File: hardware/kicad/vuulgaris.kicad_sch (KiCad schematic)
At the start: 269 parts, among them J1 TFPUSH, J10 PJ-603_C41409498, J11 TYPE-C-31-M-12, J12 FACEPLATE 2x5 IDC, J2 PJ-376, J3 PJ-376, J4 PJ-376, J5 PJ-376, J7 PJ-603_C41409498, J8 PJ-603_C41409498, J9 PJ-603_C41409498, Q1 J113 / MMBFJ113, Q2 J113 / MMBFJ113, SW1 SW_DPDT_FLAT, SW2 SW_DPDT_FLAT, SW4 12x12 tactile, SW5 12x12 tactile, SW6 12x12 tactile, SW7 12x12 tactile, SW8 12x12 tactile, SW9 12x12 tactile, U1 ES_DAISY_PATCH_SM_REV1, U101 V3205SD, U102 TL072_FLAT, U103 TL072_FLAT, U104 CD4046B, U106 TL072_FLAT, U201 V3205SD, U202 TL072_FLAT, U203 TL072_FLAT, U204 CD4046B, U206 TL072_FLAT, U3 MCP23017-E_SO, U301 TL084, U302 TL074, U4 MCP23017-E_SO, U401 TL084, U402 TL074, U5 AMS1117-3.3, U6 AMS1117-3.3, U7 DKM10E-12, U8 78L05

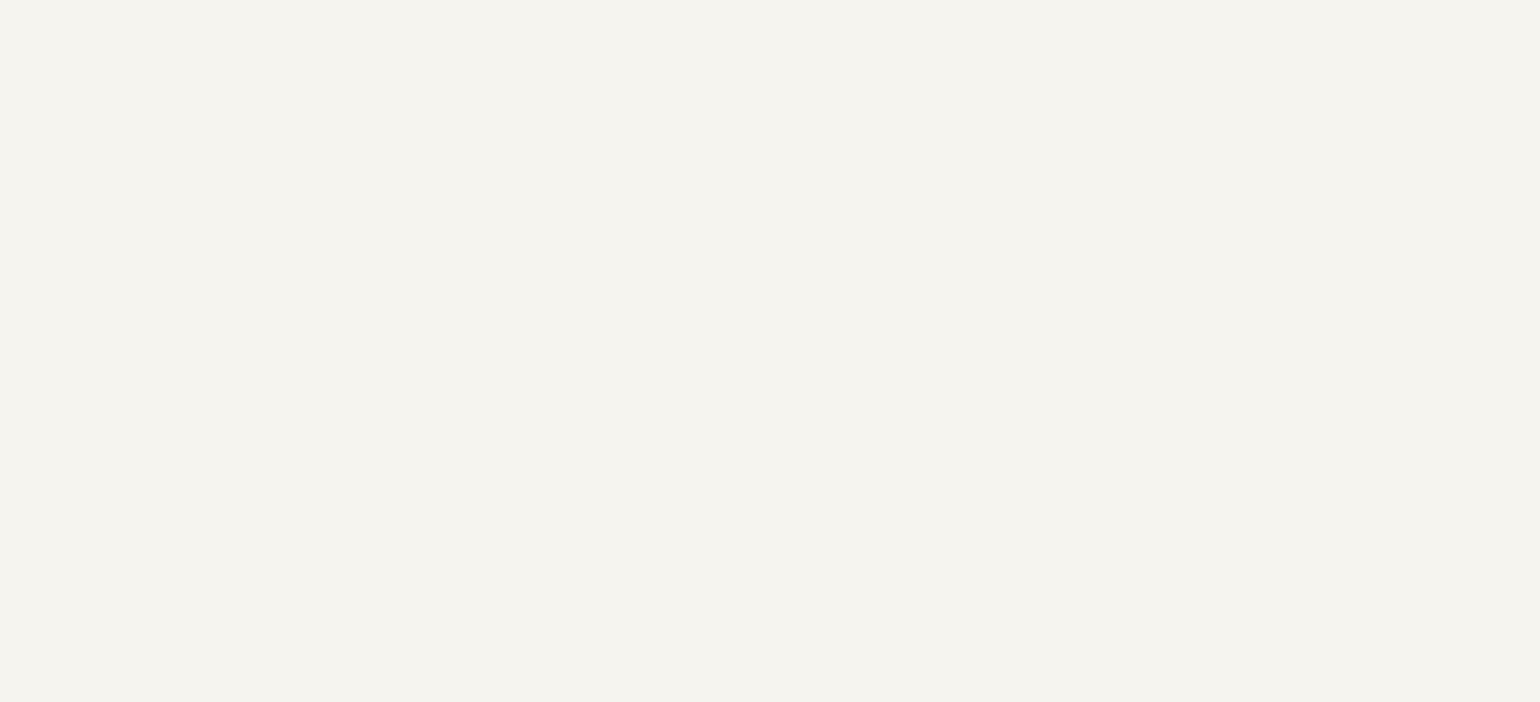
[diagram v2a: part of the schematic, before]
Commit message: hardware: ten signal test points, TP6-TP15
BBD_DRY and BBD_SIGIN per channel (the mki manual's TP1/TP3, asked for in
bbd-mki.md so R104's value can be chosen with a scope rather than by ear), the
vactrol LED drive per channel (RT301/RT401 are hand-trimmed and you cannot set a
trimmer you cannot measure), both 4046 clocks (their mistracking is the stereo
width), and the two DAC outputs (splits a fault into firmware or analog).

Placed beside the node each probes rather than in a row -- findability is the
point of a test point. 2.6-7.4mm from target.

Also re-seeded the 24 bypass caps: they had drifted to 5.0-6.1mm from their power
pin between the last placement run and this one, which the new bypass check
caught. Back to 2.1-3.1mm.

864/864 verified, 0 unintended, no pad overlaps.
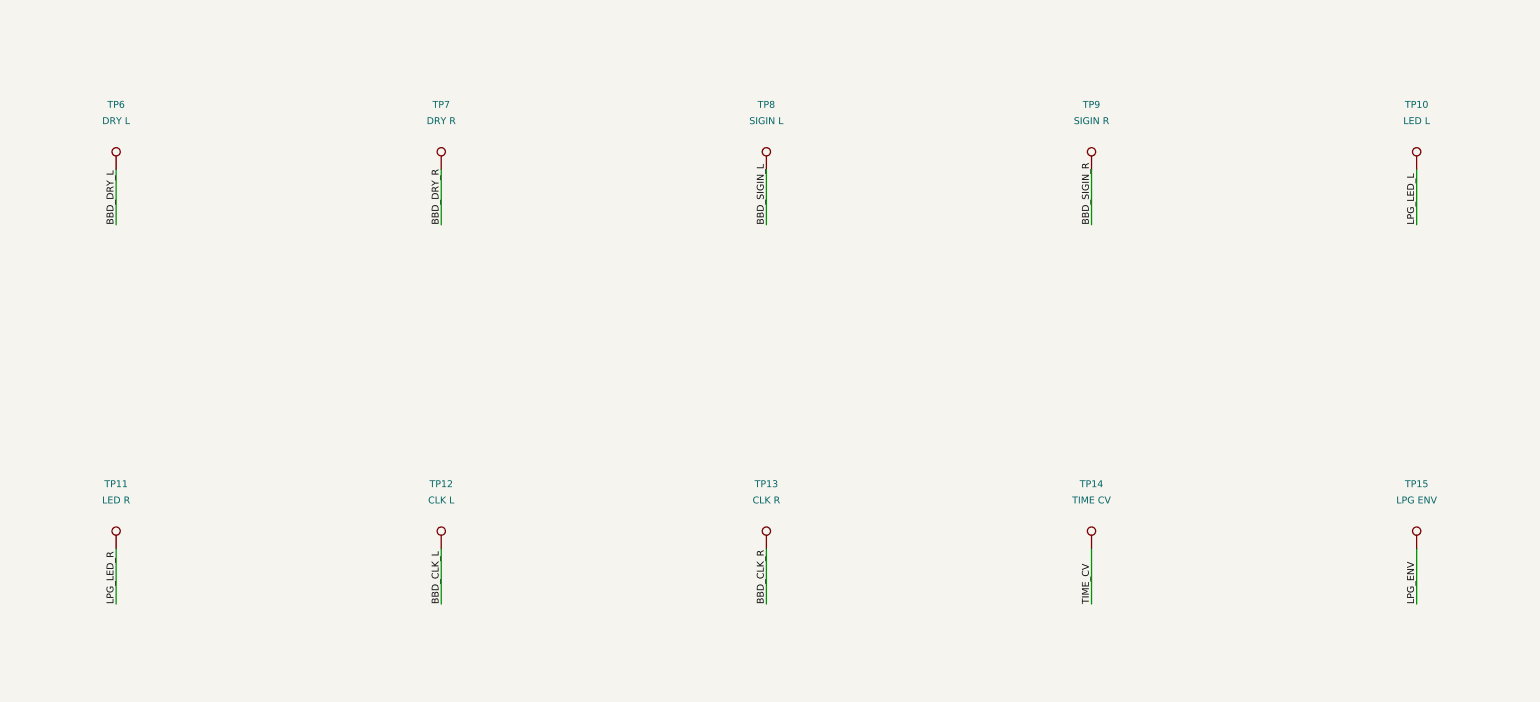
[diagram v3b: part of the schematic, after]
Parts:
- added TP10: LED L, vuulgaris:TestPoint_TH_D1.0mm, symbol vuulgaris:TestPoint
- added TP11: LED R, vuulgaris:TestPoint_TH_D1.0mm, symbol vuulgaris:TestPoint
- added TP12: CLK L, vuulgaris:TestPoint_TH_D1.0mm, symbol vuulgaris:TestPoint
- added TP13: CLK R, vuulgaris:TestPoint_TH_D1.0mm, symbol vuulgaris:TestPoint
- added TP14: TIME CV, vuulgaris:TestPoint_TH_D1.0mm, symbol vuulgaris:TestPoint
- added TP15: LPG ENV, vuulgaris:TestPoint_TH_D1.0mm, symbol vuulgaris:TestPoint
- added TP6: DRY L, vuulgaris:TestPoint_TH_D1.0mm, symbol vuulgaris:TestPoint
- added TP7: DRY R, vuulgaris:TestPoint_TH_D1.0mm, symbol vuulgaris:TestPoint
- added TP8: SIGIN L, vuulgaris:TestPoint_TH_D1.0mm, symbol vuulgaris:TestPoint
- added TP9: SIGIN R, vuulgaris:TestPoint_TH_D1.0mm, symbol vuulgaris:TestPoint
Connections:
- net BBD_CLK_L: now also TP12.1
- net BBD_CLK_R: now also TP13.1
- net BBD_DRY_L: now also TP6.1
- net BBD_DRY_R: now also TP7.1
- net BBD_SIGIN_L: now also TP8.1
- net BBD_SIGIN_R: now also TP9.1
- net LPG_ENV: now also TP15.1
- net LPG_LED_L: now also TP10.1
- net LPG_LED_R: now also TP11.1
- net TIME_CV: now also TP14.1
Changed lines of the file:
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@@
     (pin "1")
   )
+  (symbol (lib_id "vuulgaris:TestPoint") (at 1100 130 0) (unit 1)
+    (in_bom yes) (on_board yes) (dnp no)
+    (property "Reference" "TP10" (at 1100 118 0) (effects (font (size 1.27 1.27))))
+    (property "Value" "LED L" (at 1100 121 0) (effects (font (size 1.27 1.27))))
+    (property "Footprint" "vuulgaris:TestPoint_TH_D1.0mm" (at 1100 130 0) (effects (font (size 1.27 1.27)) hide))
+    (property "Datasheet" "" (at 1100 130 0) (effects (font (size 1.27 1.27)) hide))
+    (pin "1")
+  )
+  (symbol (lib_id "vuulgaris:TestPoint") (at 860 200 0) (unit 1)
+    (in_bom yes) (on_board yes) (dnp no)
+    (property "Reference" "TP11" (at 860 188 0) (effects (font (size 1.27 1.27))))
+    (property "Value" "LED R" (at 860 191 0) (effects (font (size 1.27 1.27))))
+    (property "Footprint" "vuulgaris:TestPoint_TH_D1.0mm" (at 860 200 0) (effects (font (size 1.27 1.27)) hide))
+    (property "Datasheet" "" (at 860 200 0) (effects (font (size 1.27 1.27)) hide))
+    (pin "1")
+  )
+  (symbol (lib_id "vuulgaris:TestPoint") (at 920 200 0) (unit 1)
+    (in_bom yes) (on_board yes) (dnp no)
+    (property "Reference" "TP12" (at 920 188 0) (effects (font (size 1.27 1.27))))
+    (property "Value" "CLK L" (at 920 191 0) (effects (font (size 1.27 1.27))))
+    (property "Footprint" "vuulgaris:TestPoint_TH_D1.0mm" (at 920 200 0) (effects (font (size 1.27 1.27)) hide))
+    (property "Datasheet" "" (at 920 200 0) (effects (font (size 1.27 1.27)) hide))
+    (pin "1")
+  )
+  (symbol (lib_id "vuulgaris:TestPoint") (at 980 200 0) (unit 1)
+    (in_bom yes) (on_board yes) (dnp no)
+    (property "Reference" "TP13" (at 980 188 0) (effects (font (size 1.27 1.27))))
+    (property "Value" "CLK R" (at 980 191 0) (effects (font (size 1.27 1.27))))
+    (property "Footprint" "vuulgaris:TestPoint_TH_D1.0mm" (at 980 200 0) (effects (font (size 1.27 1.27)) hide))
+    (property "Datasheet" "" (at 980 200 0) (effects (font (size 1.27 1.27)) hide))
+    (pin "1")
+  )
+  (symbol (lib_id "vuulgaris:TestPoint") (at 1040 200 0) (unit 1)
+    (in_bom yes) (on_board yes) (dnp no)
+    (property "Reference" "TP14" (at 1040 188 0) (effects (font (size 1.27 1.27))))
+    (property "Value" "TIME CV" (at 1040 191 0) (effects (font (size 1.27 1.27))))
+    (property "Footprint" "vuulgaris:TestPoint_TH_D1.0mm" (at 1040 200 0) (effects (font (size 1.27 1.27)) hide))
+    (property "Datasheet" "" (at 1040 200 0) (effects (font (size 1.27 1.27)) hide))
+    (pin "1")
+  )
+  (symbol (lib_id "vuulgaris:TestPoint") (at 1100 200 0) (unit 1)
+    (in_bom yes) (on_board yes) (dnp no)
+    (property "Reference" "TP15" (at 1100 188 0) (effects (font (size 1.27 1.27))))
+    (property "Value" "LPG ENV" (at 1100 191 0) (effects (font (size 1.27 1.27))))
+    (property "Footprint" "vuulgaris:TestPoint_TH_D1.0mm" (at 1100 200 0) (effects (font (size 1.27 1.27)) hide))
+    (property "Datasheet" "" (at 1100 200 0) (effects (font (size 1.27 1.27)) hide))
+    (pin "1")
+  )
   (symbol (lib_id "vuulgaris:TestPoint") (at 920 60 0) (unit 1)
     (in_bom yes) (on_board yes) (dnp no)
@@
     (pin "1")
   )
+  (symbol (lib_id "vuulgaris:TestPoint") (at 860 130 0) (unit 1)
+    (in_bom yes) (on_board yes) (dnp no)
+    (property "Reference" "TP6" (at 860 118 0) (effects (font (size 1.27 1.27))))
+    (property "Value" "DRY L" (at 860 121 0) (effects (font (size 1.27 1.27))))
+    (property "Footprint" "vuulgaris:TestPoint_TH_D1.0mm" (at 860 130 0) (effects (font (size 1.27 1.27)) hide))
+    (property "Datasheet" "" (at 860 130 0) (effects (font (size 1.27 1.27)) hide))
+    (pin "1")
+  )
+  (symbol (lib_id "vuulgaris:TestPoint") (at 920 130 0) (unit 1)
+    (in_bom yes) (on_board yes) (dnp no)
+    (property "Reference" "TP7" (at 920 118 0) (effects (font (size 1.27 1.27))))
+    (property "Value" "DRY R" (at 920 121 0) (effects (font (size 1.27 1.27))))
+    (property "Footprint" "vuulgaris:TestPoint_TH_D1.0mm" (at 920 130 0) (effects (font (size 1.27 1.27)) hide))
+    (property "Datasheet" "" (at 920 130 0) (effects (font (size 1.27 1.27)) hide))
+    (pin "1")
+  )
+  (symbol (lib_id "vuulgaris:TestPoint") (at 980 130 0) (unit 1)
+    (in_bom yes) (on_board yes) (dnp no)
+    (property "Reference" "TP8" (at 980 118 0) (effects (font (size 1.27 1.27))))
+    (property "Value" "SIGIN L" (at 980 121 0) (effects (font (size 1.27 1.27))))
+    (property "Footprint" "vuulgaris:TestPoint_TH_D1.0mm" (at 980 130 0) (effects (font (size 1.27 1.27)) hide))
+    (property "Datasheet" "" (at 980 130 0) (effects (font (size 1.27 1.27)) hide))
+    (pin "1")
+  )
+  (symbol (lib_id "vuulgaris:TestPoint") (at 1040 130 0) (unit 1)
+    (in_bom yes) (on_board yes) (dnp no)
+    (property "Reference" "TP9" (at 1040 118 0) (effects (font (size 1.27 1.27))))
+    (property "Value" "SIGIN R" (at 1040 121 0) (effects (font (size 1.27 1.27))))
+    (property "Footprint" "vuulgaris:TestPoint_TH_D1.0mm" (at 1040 130 0) (effects (font (size 1.27 1.27)) hide))
+    (property "Datasheet" "" (at 1040 130 0) (effects (font (size 1.27 1.27)) hide))
+    (pin "1")
+  )
   (symbol (lib_id "vuulgaris:ES_DAISY_PATCH_SM_REV1") (at 150 170 0) (unit 1)
     (in_bom yes) (on_board yes) (dnp no)
@@
   (wire (pts (xy 235.08 493.81) (xy 245.24 493.81)) (stroke (width 0) (type solid)))
   (wire (pts (xy 860.0 60.0) (xy 860.0 70.16)) (stroke (width 0) (type solid)))
+  (wire (pts (xy 1100.0 130.0) (xy 1100.0 140.16)) (stroke (width 0) (type solid)))
+  (wire (pts (xy 860.0 200.0) (xy 860.0 210.16)) (stroke (width 0) (type solid)))
+  (wire (pts (xy 920.0 200.0) (xy 920.0 210.16)) (stroke (width 0) (type solid)))
+  (wire (pts (xy 980.0 200.0) (xy 980.0 210.16)) (stroke (width 0) (type solid)))
+  (wire (pts (xy 1040.0 200.0) (xy 1040.0 210.16)) (stroke (width 0) (type solid)))
+  (wire (pts (xy 1100.0 200.0) (xy 1100.0 210.16)) (stroke (width 0) (type solid)))
   (wire (pts (xy 920.0 60.0) (xy 920.0 70.16)) (stroke (width 0) (type solid)))
   (wire (pts (xy 980.0 60.0) (xy 980.0 70.16)) (stroke (width 0) (type solid)))
   (wire (pts (xy 1040.0 60.0) (xy 1040.0 70.16)) (stroke (width 0) (type solid)))
   (wire (pts (xy 1100.0 60.0) (xy 1100.0 70.16)) (stroke (width 0) (type solid)))
+  (wire (pts (xy 860.0 130.0) (xy 860.0 140.16)) (stroke (width 0) (type solid)))
+  (wire (pts (xy 920.0 130.0) (xy 920.0 140.16)) (stroke (width 0) (type solid)))
+  (wire (pts (xy 980.0 130.0) (xy 980.0 140.16)) (stroke (width 0) (type solid)))
+  (wire (pts (xy 1040.0 130.0) (xy 1040.0 140.16)) (stroke (width 0) (type solid)))
   (wire (pts (xy 148.73 205.56) (xy 148.73 215.72)) (stroke (width 0) (type solid)))
   (wire (pts (xy 127.14 185.24) (xy 116.98 185.24)) (stroke (width 0) (type solid)))
@@
     (effects (font (size 1.27 1.27)) (justify left bottom))
   )
+  (label "LPG_LED_L" (at 1100.0 140.16 270) (fields_autoplaced)
+    (effects (font (size 1.27 1.27)) (justify left bottom))
+  )
+  (label "LPG_LED_R" (at 860.0 210.16 270) (fields_autoplaced)
+    (effects (font (size 1.27 1.27)) (justify left bottom))
+  )
+  (label "BBD_CLK_L" (at 920.0 210.16 270) (fields_autoplaced)
+    (effects (font (size 1.27 1.27)) (justify left bottom))
+  )
+  (label "BBD_CLK_R" (at 980.0 210.16 270) (fields_autoplaced)
+    (effects (font (size 1.27 1.27)) (justify left bottom))
+  )
+  (label "TIME_CV" (at 1040.0 210.16 270) (fields_autoplaced)
+    (effects (font (size 1.27 1.27)) (justify left bottom))
+  )
+  (label "LPG_ENV" (at 1100.0 210.16 270) (fields_autoplaced)
+    (effects (font (size 1.27 1.27)) (justify left bottom))
+  )
   (label "NEG12V" (at 920.0 70.16 270) (fields_autoplaced)
     (effects (font (size 1.27 1.27)) (justify left bottom))
@@
     (effects (font (size 1.27 1.27)) (justify left bottom))
   )
+  (label "BBD_DRY_L" (at 860.0 140.16 270) (fields_autoplaced)
+    (effects (font (size 1.27 1.27)) (justify left bottom))
+  )
+  (label "BBD_DRY_R" (at 920.0 140.16 270) (fields_autoplaced)
+    (effects (font (size 1.27 1.27)) (justify left bottom))
+  )
+  (label "BBD_SIGIN_L" (at 980.0 140.16 270) (fields_autoplaced)
+    (effects (font (size 1.27 1.27)) (justify left bottom))
+  )
+  (label "BBD_SIGIN_R" (at 1040.0 140.16 270) (fields_autoplaced)
+    (effects (font (size 1.27 1.27)) (justify left bottom))
+  )

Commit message: hardware: LPG trimmers to SMD 3224W, mounted on the back
RT301/RT401 go from Bourns 3266W (through-hole, no LCSC number at all) to
3224W-1-203E, LCSC C55071 -- the SMD sibling: same 4mm square multiturn cermet,
12 turns, top-adjust, 9784 in stock. Footprint pulled with easyeda2kicad. Pin
numbering matches TRIMPOT_3T, so the rheostat wiring is unchanged.

Multiturn was the constraint. These set vactrol LED drive depth by ear against a
scope; the 3x3mm single-turn parts are cheaper and better stocked but put 20k
into 270 degrees.

Mounted on B.Cu rather than with the rest of the LPG on F.Cu: the front is under
the faceplate, so a top-adjust trimmer there is only reachable with the panel
off, and vactrols age. Flip verified against the library by place.py's pad
orientation check (700 pads, 0 wrong) and in the plotted gerbers (3 B.Cu flashes
at RT301).

Takes the hand-solder list from 12 parts to 10; what remains has no LCSC source.

864/864 verified, no pad overlaps, nothing within 1.5mm of a chip pad.
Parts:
- RT301, RT401: footprint vuulgaris:Potentiometer_Bourns_3266W_Vertical -> vuulgaris:RES-ADJ-SMD_3224W
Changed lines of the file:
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@@
     (property "Reference" "RT301" (at 520 3888 0) (effects (font (size 1.27 1.27))))
     (property "Value" "20k trim" (at 520 3891 0) (effects (font (size 1.27 1.27))))
-    (property "Footprint" "vuulgaris:Potentiometer_Bourns_3266W_Vertical" (at 520 3900 0) (effects (font (size 1.27 1.27)) hide))
+    (property "Footprint" "vuulgaris:RES-ADJ-SMD_3224W" (at 520 3900 0) (effects (font (size 1.27 1.27)) hide))
     (property "Datasheet" "" (at 520 3900 0) (effects (font (size 1.27 1.27)) hide))
     (pin "1")
@@
     (property "Reference" "RT401" (at 720 3888 0) (effects (font (size 1.27 1.27))))
     (property "Value" "20k trim" (at 720 3891 0) (effects (font (size 1.27 1.27))))
-    (property "Footprint" "vuulgaris:Potentiometer_Bourns_3266W_Vertical" (at 720 3900 0) (effects (font (size 1.27 1.27)) hide))
+    (property "Footprint" "vuulgaris:RES-ADJ-SMD_3224W" (at 720 3900 0) (effects (font (size 1.27 1.27)) hide))
     (property "Datasheet" "" (at 720 3900 0) (effects (font (size 1.27 1.27)) hide))
     (pin "1")

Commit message: hardware: headphone monitor output -- OPA1688 driver and J6
J6 (PJ-376, already a stereo TRS: 1 sleeve, 2 ring, 3 tip) on the top wall
immediately right of J10, tucked under the OLED on B.Cu as J9/J10 already are.

U9 is an OPA1688 (C206212) rather than the NJM4556A first proposed -- same
supply range and 75mA drive, but TI characterise 0.00005 percent THD+N INTO 32
ohms and TIPD189 is their headphone-amp reference design on it. Two orders of
magnitude better distortion.

Its LCSC symbol is multi-unit (pins 1/7, 2/6, 3/5 share coordinates) and would
have stubbed OUTA onto OUTB in mksch, so OPA1688_FLAT is cloned from TL072_FLAT,
whose pinout is identical. Same trap the other FLAT symbols exist for.

Taps BBD_OUT -- what the quarter-inch jacks and the resample leg see -- through
1uF, 100k, a 20k trimmer to ground, a unity buffer and 22R. Max ratio 0.167,
roughly 10mW into 32 ohms; the trimmers bring it down and are set once. No
dual-gang SMD trimmer is in stock anywhere, so there are two, against bbd-mki's
advice about L/R matching: set them with a meter, not by ear.

Two things the placement seeds cannot express, fixed in the board:

- the block belongs on B.Cu; seeded parts arrive on F.Cu and sat on the OLED
- J6 needs rotation -90 like every other jack. At rotation 0 the PJ-376 body
  runs 24mm in -x and lands on J10 -- caught by the body-overlap check. The
  pad-orientation check then caught that rotating a footprint also has to update
  its stored ABSOLUTE pad angles: J5 stores 270, J6 had 0, and the pads are
  1.6x3.1 rectangles so the difference is real copper.

897/897 verified, 0 unintended. Body overlaps back to the three pre-existing.
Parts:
- added C505, C506: 1uF film, vuulgaris:C0603, symbol vuulgaris:C
- added C507, C508: 100nF, vuulgaris:C0603, symbol vuulgaris:C
- added J6: PJ-376, vuulgaris:AUDIO-TH_PJ-376, symbol vuulgaris:PJ-376
- added R509, R510: 100k, vuulgaris:R0603, symbol vuulgaris:R
- added R511, R512: 22R, vuulgaris:R0603, symbol vuulgaris:R
- added RT501, RT502: 20k trim, vuulgaris:RES-ADJ-SMD_3224W, symbol vuulgaris:TRIMPOT_3T
- added U9: OPA1688_FLAT, vuulgaris:SOP-8_L4.9-W3.9-P1.27-LS6.0-BL, symbol vuulgaris:OPA1688_FLAT
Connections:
- net BBD_OUT_L: now also C505.1
- net BBD_OUT_R: now also C506.1
- net GND: now also C507.2, C508.2, J6.1, RT501.3, RT502.3
- net NEG12V: now also C508.1, U9.4 (V-)
- net POS12V: now also C507.1, U9.8 (V+)
- new net HP_BUF_L: R511.1, U9.1 (1OUT), U9.2 (1IN-)
- new net HP_BUF_R: R512.1, U9.6 (2IN-), U9.7 (2OUT)
- new net HP_DIV_L: R509.2, RT501.1
- new net HP_DIV_R: R510.2, RT502.1
- new net HP_IN_L: C505.2, R509.1
- new net HP_IN_R: C506.2, R510.1
- new net HP_OUT_L: J6.3, R511.2
- new net HP_OUT_R: J6.2, R512.2
- new net HP_W_L: RT501.2 (WIPER), U9.3 (1IN+)
- new net HP_W_R: RT502.2 (WIPER), U9.5 (2IN+)
